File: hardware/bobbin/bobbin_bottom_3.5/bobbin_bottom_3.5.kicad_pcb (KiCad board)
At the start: 2 copper layers, 68.5 x 8.5 mm, 5 parts, among them J1 OC, J2 OC, J3 IC, J4 IC

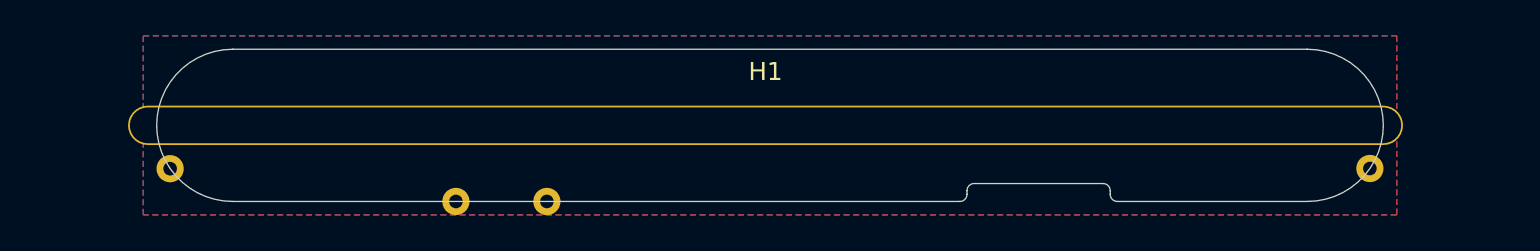
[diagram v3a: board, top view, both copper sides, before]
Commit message: 3.5" and 4.0" bottom bobbin PCB layout
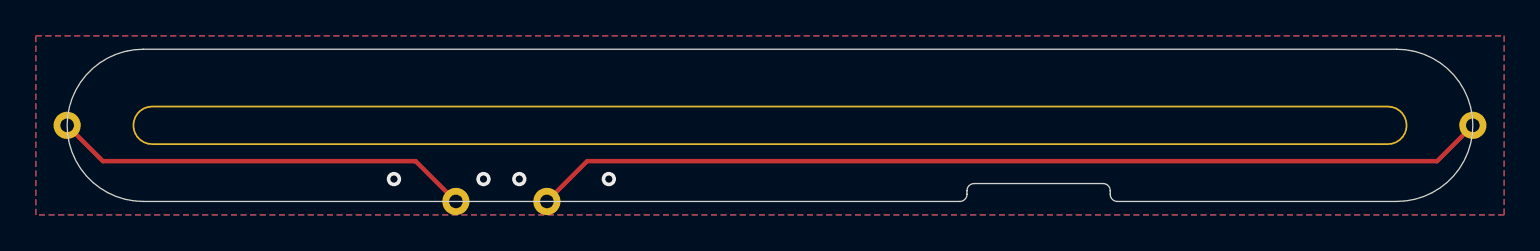
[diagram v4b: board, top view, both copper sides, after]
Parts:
- moved J3 6.24 mm to (90.8, 101.0)
- moved J2 6.23 mm to (169.2, 101.0)
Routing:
- net /OC: track 0.00 -> 53.5 mm
- net /IC: track 0.00 -> 23.5 mm
- net GND: vias 0 -> 4
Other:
- board size 68.5 x 8.5 mm -> 78.5 x 8.5 mm
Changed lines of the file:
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@@
   )
   (footprint "cycfi_library:single-pad-1.52x1.52-th" (layer "F.Cu")
-    (at 163.5 103.41 180)
+    (at 169.25 101 180)
     (property "Sheetfile" "bobbin_bottom_3.5.kicad_sch")
     (property "Sheetname" "")
@@
   )
   (footprint "cycfi_library:single-pad-1.52x1.52-th" (layer "F.Cu")
-    (at 96.5 103.42)
+    (at 90.75 101)
     (property "Sheetfile" "bobbin_bottom_3.5.kicad_sch")
     (property "Sheetname" "")
@@
     (property "Sheetname" "")
     (attr through_hole)
-    (fp_text reference "H1" (at 0 -3 unlocked) (layer "F.SilkS")
+    (fp_text reference "H1" (at 0 -3 unlocked) (layer "F.SilkS") hide
       (effects (font (size 1 1) (thickness 0.15)))
     )
@@
       (effects (font (size 1 1) (thickness 0.15)))
     )
-    (pad "1" thru_hole oval (at 0 0) (size 71.2 2.2) (drill oval 71 2) (layers *.Cu *.Mask)
+    (pad "1" thru_hole oval (at 0.25 0) (size 71.2 2.2) (drill oval 71 2) (layers *.Cu *.Mask)
       (net 1 "GND") (pinfunction "1") (pintype "input"))
   )
@@
       (net 3 "/IC") (pinfunction "Pin_1") (pintype "passive"))
   )
-  (gr_arc (start 149.4 105.25) (mid 149.117157 105.132843) (end 149 104.85) (layer "Dwgs.User") (width 0.01))
-  (gr_arc (start 160 96.75) (mid 164.25 101) (end 160 105.25) (layer "Dwgs.User") (width 0.01))
-  (gr_line (start 100 100) (end 100 102) (layer "Dwgs.User") (width 0.01))
-  (gr_line (start 100 96.75) (end 160 96.75) (layer "Dwgs.User") (width 0.01))
-  (gr_line (start 100 102) (end 160 102) (layer "Dwgs.User") (width 0.01))
-  (gr_arc (start 141 104.65) (mid 141.117157 104.367157) (end 141.4 104.25) (layer "Dwgs.User") (width 0.01))
+  (gr_arc (start 165 96.75) (mid 169.25 101) (end 165 105.25) (layer "Dwgs.User") (width 0.01))
+  (gr_line (start 95 100) (end 95 102) (layer "Dwgs.User") (width 0.01))
+  (gr_arc (start 95 105.25) (mid 90.75 101) (end 95 96.75) (layer "Dwgs.User") (width 0.01))
+  (gr_line (start 140.6 105.25) (end 95 105.25) (layer "Dwgs.User") (width 0.01))
+  (gr_arc (start 116.778 105.25) (mid 117.54 104.488) (end 118.302 105.25) (layer "Dwgs.User") (width 0.01))
+  (gr_line (start 165 100) (end 165 102) (layer "Dwgs.User") (width 0.01))
   (gr_arc (start 148.6 104.25) (mid 148.882843 104.367157) (end 149 104.65) (layer "Dwgs.User") (width 0.01))
   (gr_arc (start 111.698 105.25) (mid 112.46 104.488) (end 113.222 105.25) (layer "Dwgs.User") (width 0.01))
+  (gr_arc (start 141 104.65) (mid 141.117157 104.367157) (end 141.4 104.25) (layer "Dwgs.User") (width 0.01))
+  (gr_arc (start 90.818311 100.241068) (mid 91.512 101) (end 90.818311 101.758932) (layer "Dwgs.User") (width 0.01))
+  (gr_line (start 141.4 104.25) (end 148.6 104.25) (layer "Dwgs.User") (width 0.01))
+  (gr_line (start 95 96.75) (end 165 96.75) (layer "Dwgs.User") (width 0.01))
+  (gr_line (start 141 104.85) (end 141 104.65) (layer "Dwgs.User") (width 0.01))
+  (gr_arc (start 169.181689 101.758932) (mid 168.488 101) (end 169.181689 100.241068) (layer "Dwgs.User") (width 0.01))
+  (gr_line (start 165 105.25) (end 149.4 105.25) (layer "Dwgs.User") (width 0.01))
+  (gr_line (start 95 100) (end 165 100) (layer "Dwgs.User") (width 0.01))
+  (gr_arc (start 149.4 105.25) (mid 149.117157 105.132843) (end 149 104.85) (layer "Dwgs.User") (width 0.01))
   (gr_line (start 149 104.65) (end 149 104.85) (layer "Dwgs.User") (width 0.01))
-  (gr_arc (start 116.778 105.25) (mid 117.54 104.488) (end 118.302 105.25) (layer "Dwgs.User") (width 0.01))
-  (gr_line (start 160 105.25) (end 149.4 105.25) (layer "Dwgs.User") (width 0.01))
-  (gr_line (start 141 104.85) (end 141 104.65) (layer "Dwgs.User") (width 0.01))
-  (gr_line (start 160 100) (end 160 102) (layer "Dwgs.User") (width 0.01))
-  (gr_arc (start 96.125734 102.747159) (mid 97.12753 102.978649) (end 96.986778 103.997164) (layer "Dwgs.User") (width 0.01))
-  (gr_line (start 100 100) (end 160 100) (layer "Dwgs.User") (width 0.01))
+  (gr_line (start 95 102) (end 165 102) (layer "Dwgs.User") (width 0.01))
   (gr_arc (start 141 104.85) (mid 140.882843 105.132843) (end 140.6 105.25) (layer "Dwgs.User") (width 0.01))
-  (gr_line (start 140.6 105.25) (end 100 105.25) (layer "Dwgs.User") (width 0.01))
-  (gr_arc (start 163.013222 103.997164) (mid 162.872472 102.97865) (end 163.874266 102.747159) (layer "Dwgs.User") (width 0.01))
-  (gr_arc (start 100 105.25) (mid 95.75 101) (end 100 96.75) (layer "Dwgs.User") (width 0.01))
-  (gr_line (start 141.4 104.25) (end 148.6 104.25) (layer "Dwgs.User") (width 0.01))
+  (gr_arc (start 165 96.75) (mid 169.25 101) (end 165 105.25) (layer "Edge.Cuts") (width 0.01))
+  (gr_arc (start 141 104.85) (mid 140.882843 105.132843) (end 140.6 105.25) (layer "Edge.Cuts") (width 0.01))
+  (gr_line (start 165 105.25) (end 149.4 105.25) (layer "Edge.Cuts") (width 0.01))
+  (gr_arc (start 95 105.25) (mid 90.75 101) (end 95 96.75) (layer "Edge.Cuts") (width 0.01))
+  (gr_line (start 95 96.75) (end 165 96.75) (layer "Edge.Cuts") (width 0.01))
   (gr_arc (start 148.6 104.25) (mid 148.882843 104.367157) (end 149 104.65) (layer "Edge.Cuts") (width 0.01))
+  (gr_arc (start 149.4 105.25) (mid 149.117157 105.132843) (end 149 104.85) (layer "Edge.Cuts") (width 0.01))
+  (gr_line (start 149 104.65) (end 149 104.85) (layer "Edge.Cuts") (width 0.01))
   (gr_line (start 141 104.85) (end 141 104.65) (layer "Edge.Cuts") (width 0.01))
-  (gr_line (start 149 104.65) (end 149 104.85) (layer "Edge.Cuts") (width 0.01))
-  (gr_arc (start 141 104.85) (mid 140.882843 105.132843) (end 140.6 105.25) (layer "Edge.Cuts") (width 0.01))
+  (gr_line (start 141.4 104.25) (end 148.6 104.25) (layer "Edge.Cuts") (width 0.01))
   (gr_arc (start 141 104.65) (mid 141.117157 104.367157) (end 141.4 104.25) (layer "Edge.Cuts") (width 0.01))
-  (gr_line (start 100 96.75) (end 160 96.75) (layer "Edge.Cuts") (width 0.01))
-  (gr_arc (start 100 105.25) (mid 95.75 101) (end 100 96.75) (layer "Edge.Cuts") (width 0.01))
-  (gr_line (start 141.4 104.25) (end 148.6 104.25) (layer "Edge.Cuts") (width 0.01))
-  (gr_arc (start 149.4 105.25) (mid 149.117157 105.132843) (end 149 104.85) (layer "Edge.Cuts") (width 0.01))
-  (gr_line (start 140.6 105.25) (end 100 105.25) (layer "Edge.Cuts") (width 0.01))
-  (gr_line (start 160 105.25) (end 149.4 105.25) (layer "Edge.Cuts") (width 0.01))
-  (gr_arc (start 160 96.75) (mid 164.25 101) (end 160 105.25) (layer "Edge.Cuts") (width 0.01))
+  (gr_line (start 140.6 105.25) (end 95 105.25) (layer "Edge.Cuts") (width 0.01))
+  (via (at 109 104) (size 0.8) (drill 0.4) (layers "F.Cu" "B.Cu") (free) (net 1))
+  (via (at 114 104) (size 0.8) (drill 0.4) (layers "F.Cu" "B.Cu") (free) (net 1))
+  (via (at 116 104) (size 0.8) (drill 0.4) (layers "F.Cu" "B.Cu") (free) (net 1))
+  (via (at 121 104) (size 0.8) (drill 0.4) (layers "F.Cu" "B.Cu") (free) (net 1))
+  (segment (start 117.54 105.25) (end 119.79 103) (width 0.25) (layer "F.Cu") (net 2))
+  (segment (start 119.79 103) (end 167.25 103) (width 0.25) (layer "F.Cu") (net 2))
+  (segment (start 167.25 103) (end 169.25 101) (width 0.25) (layer "F.Cu") (net 2))
+  (segment (start 110.21 103) (end 92.75 103) (width 0.25) (layer "F.Cu") (net 3))
+  (segment (start 112.46 105.25) (end 110.21 103) (width 0.25) (layer "F.Cu") (net 3))
+  (segment (start 92.75 103) (end 90.75 101) (width 0.25) (layer "F.Cu") (net 3))
   (zone (net 1) (net_name "GND") (layer "F.Cu") (hatch edge 0.508)
     (connect_pads (clearance 0.25))
     (min_thickness 0.254) (filled_areas_thickness no)
-    (fill (thermal_gap 0.508) (thermal_bridge_width 0.508))
+    (fill yes (thermal_gap 0.508) (thermal_bridge_width 0.508))
     (polygon
       (pts
-        (xy 165 106)
-        (xy 95 106)
-        (xy 95 96)
-        (xy 165 96)
+        (xy 171 106)
+        (xy 89 106)
+        (xy 89 96)
+        (xy 171 96)
       )
     )
@@
     (connect_pads (clearance 0.25))
     (min_thickness 0.254) (filled_areas_thickness no)
-    (fill (thermal_gap 0.508) (thermal_bridge_width 0.508))
+    (fill yes (thermal_gap 0.508) (thermal_bridge_width 0.508))
     (polygon
       (pts
-        (xy 165 106)
-        (xy 95 106)
-        (xy 95 96)
-        (xy 165 96)
+        (xy 171 106)
+        (xy 89 106)
+        (xy 89 96)
+        (xy 171 96)
       )
     )
